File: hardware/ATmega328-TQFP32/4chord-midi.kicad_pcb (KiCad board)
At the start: 2 copper layers, 75 x 85 mm, 63 parts, among them IC1 ATMEGA328P-A, P1 USB_B, P2 Programmer, P3 UART, Q1 2N2222, SW1 <, SW2 Select, SW3 >, SW4 I, SW5 V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

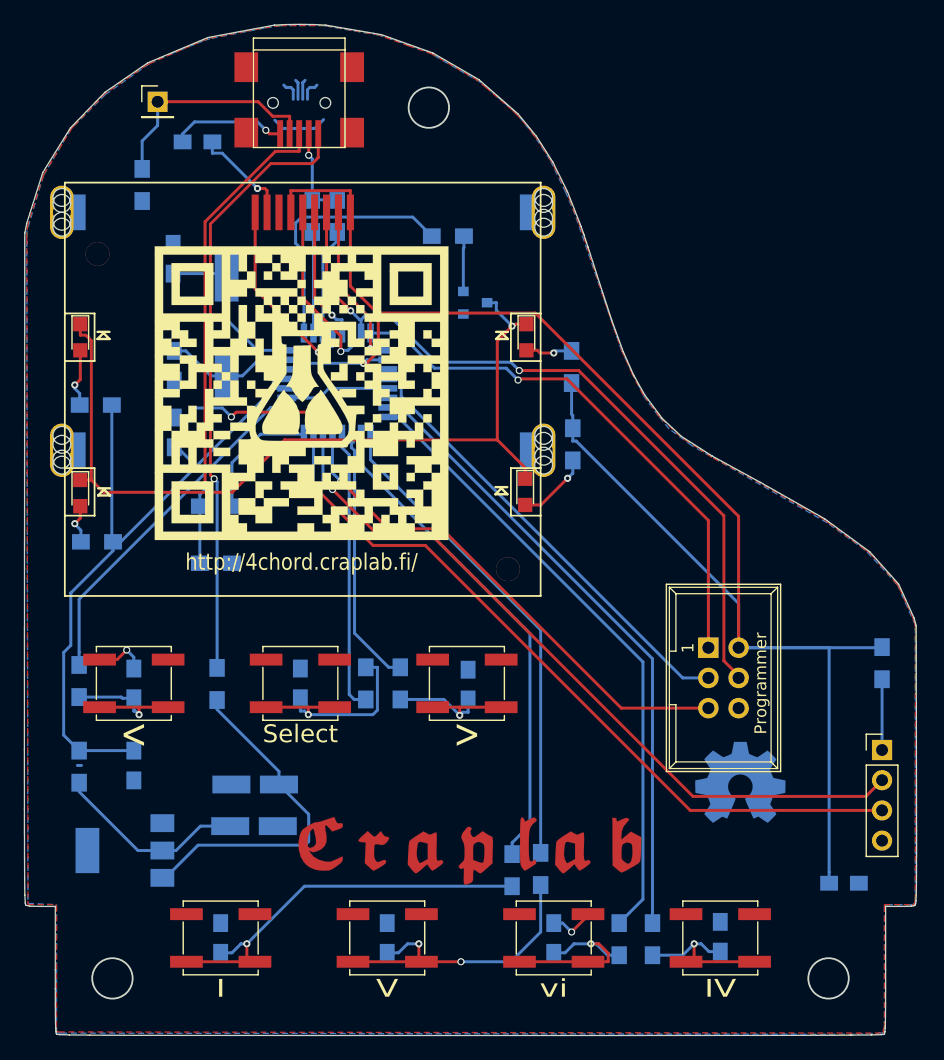
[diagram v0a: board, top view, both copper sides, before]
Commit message: issue-#13: Revised Revision B hardware
Reworked schematic to separate to logical blocks, added reset circuit,
fixed Q1 pin assignment and changed it from BJT to MOSFET component.
Also added power supply choices for UART (5V, 3.3V and none) and a
fourth rubber foot for better balance.

Obviously same changes in the PCB design, also moved button silk screen
bit more down for better readability. Fixed one sharp corner in the
board border. Improved routing somewhat.
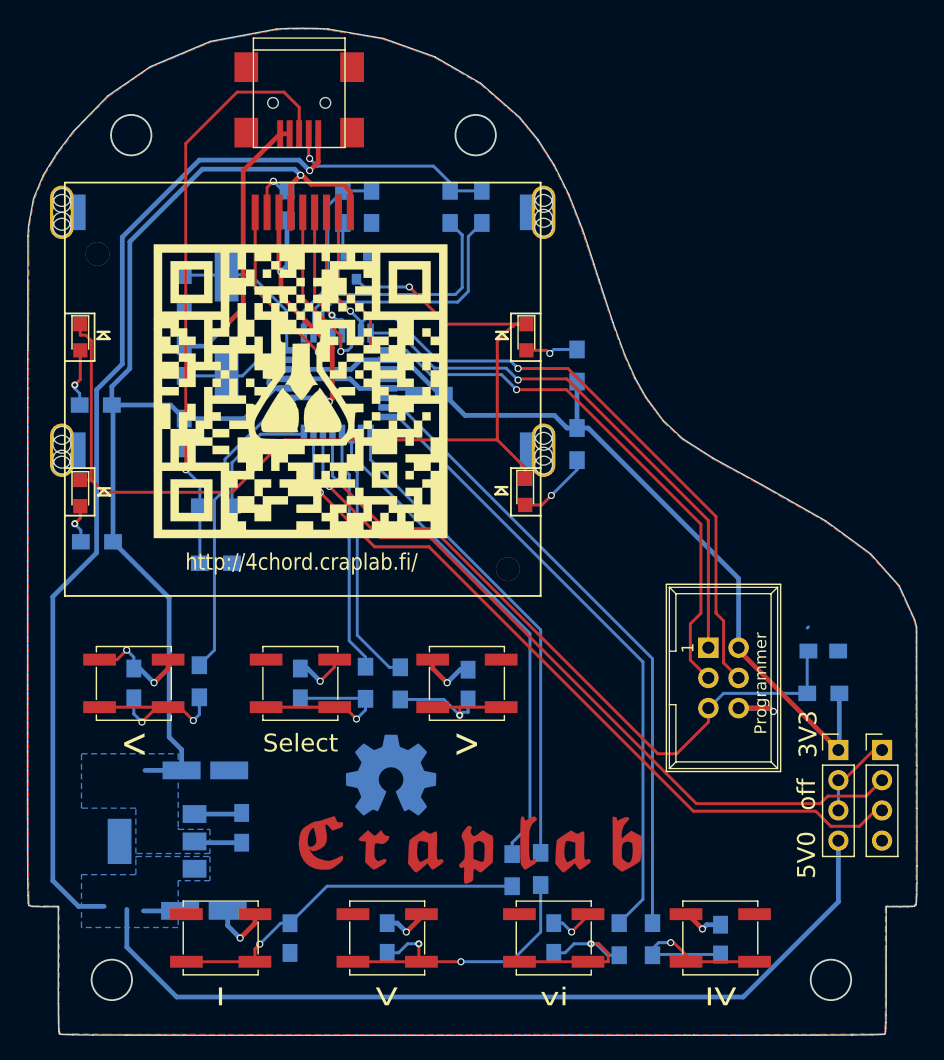
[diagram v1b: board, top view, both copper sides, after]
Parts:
- removed the G*** at (159.2, 118.8)
- removed G10: LOGO, Artwork_4chord-midi:projpage-QR-code-inv
- removed the G4 at (173.0, 121.0)
- removed the G4 at (146.2, 118.2)
- removed G5: LOGO, Artwork_4chord-midi:oshw-mask
- removed R19, R20: 0R, Resistors_SMD:R_0805_HandSoldering
- removed W1: TP, Pin_Headers:Pin_Header_Straight_1x01_Pitch2.54mm
- added C16: 100n, Capacitors_SMD:C_0805_HandSoldering, B.Cu at (180.0, 110.0)
- added G***: LOGO, Artwork_4chord-midi:craplab-2400, B.Cu at (176.5, 103.0)
- added G11: qr, Artwork_4chord-midi:projpage-QR-code-inv, F.Cu at (136.0, 88.1)
- added G12: 4chordmidi, Artwork_4chord-midi:4chord-midi, B.Cu at (142.1, 101.2)
- added G22: craplab, Artwork_4chord-midi:craplab, B.Cu at (166.0, 101.6)
- added G31: finland, Artwork_4chord-midi:finland, B.Cu at (164.0, 119.4)
- added G4: LOGO, Artwork_4chord-midi:oshw-cooper, B.Cu at (143.6, 120.4)
- added P4: UART Power, Pin_Headers:Pin_Header_Straight_1x04_Pitch2.54mm, F.Cu at (181.2, 118.3)
- G1: footprint Artwork_4chord-midi:craplab-fraktur-Cu -> Artwork_4chord-midi:craplab-fraktur-Mask
- G2: footprint Artwork_4chord-midi:craplab-fraktur-Mask -> Artwork_4chord-midi:craplab-fraktur-Cu
- G3: footprint Artwork_4chord-midi:4chord-midi -> Artwork_4chord-midi:oshw-mask
- Q1: value 2N2222 -> 2N7002
- R16: value 1k -> 100
- R17: value 0R -> 1M
- R18: value 0R -> 10k
- moved C4 53.9 mm to (146.8, 88.4), turned to 180 degrees
- moved R18 51.0 mm to (180.0, 113.5), turned to 180 degrees
- moved C3 33.7 mm to (131.1, 124.8)
- moved C5 28.2 mm to (126.2, 91.7)
- moved G3 19.4 mm to (143.6, 120.4)
- moved R17 19.4 mm to (142.0, 72.6)
- moved R3 12.2 mm to (151.3, 72.6)
- moved R1 11.6 mm to (148.6, 72.6)
- moved C1 11.5 mm to (127.9, 131.8), turned to 0 degrees
- moved Q1 10.4 mm to (140.7, 77.7), turned to 270 degrees
- moved R5 10.1 mm to (127.5, 112.5)
- moved C15 9.23 mm to (134.9, 72.5), turned to 270 degrees
- moved R16 9.16 mm to (139.6, 72.6), turned to 90 degrees
- moved C2 6.22 mm to (128.0, 120.0)
- moved C11 5.83 mm to (135.1, 134.1), turned to 270 degrees
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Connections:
- net /BTN_MENU_MINUS renamed /BTN_MENU_PREV
- net /BTN_MENU_PLUS renamed /BTN_MENU_NEXT
- C1 pad 1: Net-(C1-Pad1) -> +5V
- C2 pad 1: Net-(C2-Pad1) -> +3V3
- P1 pad 1: Net-(P1-Pad1) -> +5V
- P1 pad 4: Net-(P1-Pad4) -> GND
- Q1 pad 1: GND -> Net-(Q1-Pad1)
- Q1 pad 2: Net-(Q1-Pad2) -> GND
- R16 pad 1: Net-(Q1-Pad2) -> Net-(Q1-Pad1)
- R17 pad 1: Net-(P1-Pad4) -> /LCD_BACKLIGHT_PWM
- R18 pad 1: Net-(C1-Pad1) -> +3V3
- R18 pad 2: Net-(P1-Pad1) -> /#RESET
- U1 pad 2: Net-(C2-Pad1) -> +3V3
- U1 pad 3: Net-(C1-Pad1) -> +5V
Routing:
- net +5V: track 0.00 -> 160.6 mm, vias 0 -> 1
- net GND: track 41.9 -> 105.9 mm, vias 5 -> 12
- net Net-(P1-Pad1): track 50.9 -> 0.00 mm, vias 1 -> 0
- net +3V3: track 210.9 -> 177.7 mm
- net Net-(C1-Pad1): track 28.7 -> 0.00 mm
- net Net-(P1-Pad4): track 19.3 -> 0.00 mm
- net /#RESET: track 43.0 -> 59.9 mm
- net Net-(C2-Pad1): track 16.3 -> 0.00 mm
- net Net-(D1-Pad1): track 69.9 -> 82.5 mm
- net /USB_D-: track 8.54 -> 21.1 mm
- net /USB_RESET: track 9.00 -> 21.0 mm
- net (no net): track 11.9 -> 0.14 mm
- net Net-(P1-Pad2): track 7.77 -> 18.1 mm
- net Net-(P1-Pad3): track 40.7 -> 49.9 mm
- net /LCD_BACKLIGHT_PWM: track 21.9 -> 15.8 mm
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- added copper zone on B.Cu, net +3V3
- added copper zone on B.Cu, net +5V
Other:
- board size 75 x 85 mm -> 74.8 x 84.7 mm
- net class Power added: clearance 0.2, trace_width 0.4, via_dia 0.6, via_drill 0.4
- net class Signal added: clearance 0.2, trace_width 0.2, via_dia 0.6, via_drill 0.4
- board text added: "08-2017"
- board text added: "3V3"
- board text added: "5V0"
- board text added: "Designed in Finland, perkele!"
- board text added: "off"
- board text removed: "----------------------- Zero Ohm debug links: ----------------------- R17: GND R18: 5V USB input voltage Vbus R19: 3.3V LDO output voltage Vout ----------------------- R20: UART Vin, DNP for USB UART -----------------------"
- board text removed: "07-2017"

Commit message: issue-#15 Finalized Revision B hardware
Final little touches here and there on the PCB design, mainly silk
screen adjustments and moved the upper rubber feet.

Alos, fucked up 00f85adde54214f45f219a16524527a8af92649b which should
have been linked to issue-#15 as well. Oh well..
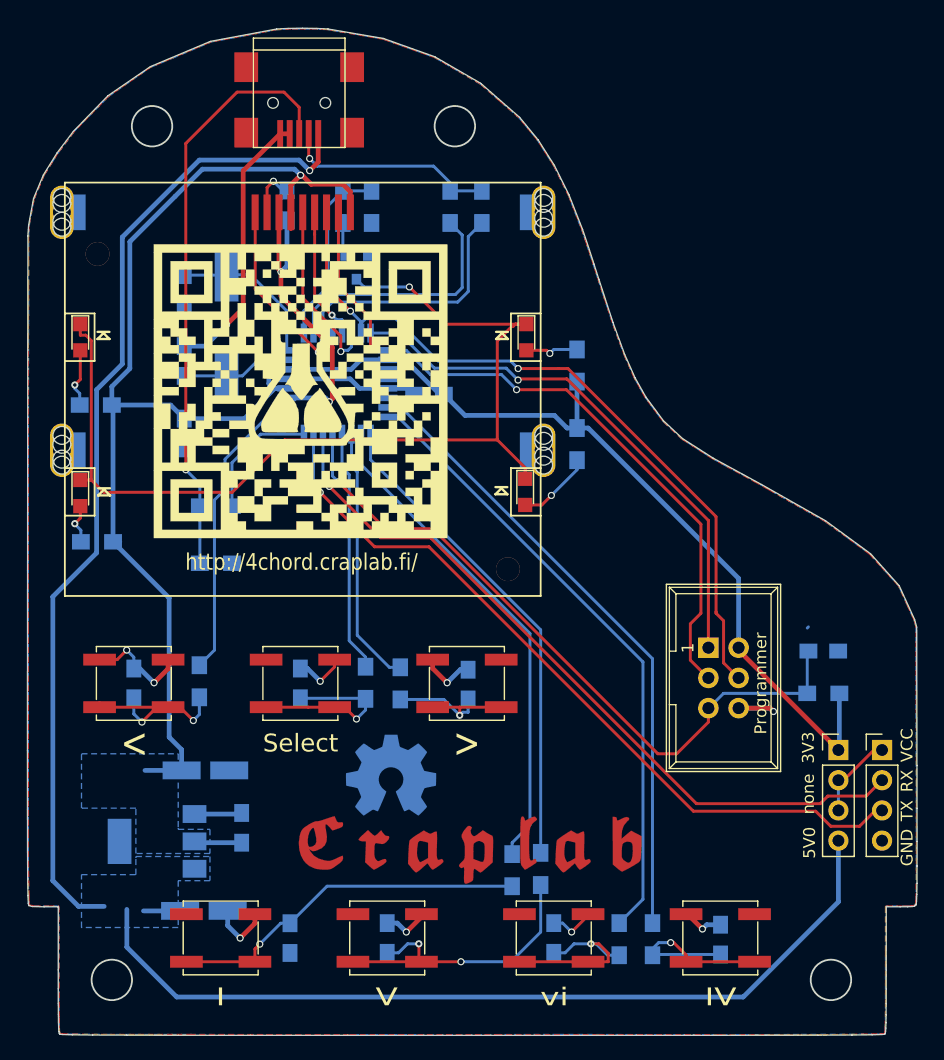
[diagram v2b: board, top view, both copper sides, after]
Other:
- outline, holes or cut-outs redrawn
- board text added: "GND"
- board text added: "RX"
- board text added: "TX"
- board text added: "VCC"
- board text added: "none"
- board text removed: "off"
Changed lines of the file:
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@@
     (area 113.004021 57.572699 187.894301 142.340801)
     (thickness 1.6)
-    (drawings 128)
+    (drawings 132)
     (tracks 471)
     (zones 0)
@@
     (zone_45_only yes)
     (trace_min 0.2)
-    (segment_width 0.2)
+    (segment_width 0.15)
     (edge_width 0.15)
     (via_size 0.6)
@@
       (xy -0.560917 0.037042)) (layer B.SilkS) (width 0.01))
   )
-  (gr_text off (at 178.562 122.047 90) (layer F.SilkS)
-    (effects (font (size 1.5 1.5) (thickness 0.3)))
+  (gr_text VCC (at 187 117.9 90) (layer F.SilkS)
+    (effects (font (size 1 1) (thickness 0.2)))
   )
-  (gr_text 3V3 (at 178.689 116.967 90) (layer F.SilkS)
-    (effects (font (size 1.5 1.5) (thickness 0.3)))
+  (gr_text RX (at 187 120.9 90) (layer F.SilkS)
+    (effects (font (size 1 1) (thickness 0.2)))
   )
-  (gr_text 5V0 (at 178.562 127.127 90) (layer F.SilkS)
-    (effects (font (size 1.5 1.5) (thickness 0.3)))
+  (gr_text TX (at 187 123.4 90) (layer F.SilkS)
+    (effects (font (size 1 1) (thickness 0.2)))
+  )
+  (gr_text GND (at 187 126.5 90) (layer F.SilkS)
+    (effects (font (size 1 1) (thickness 0.2)))
+  )
+  (gr_text none (at 178.7 122 90) (layer F.SilkS)
+    (effects (font (size 1 1) (thickness 0.2)))
+  )
+  (gr_text 3V3 (at 178.7 118.1 90) (layer F.SilkS)
+    (effects (font (size 1 1) (thickness 0.2)))
+  )
+  (gr_text 5V0 (at 178.8 126.1 90) (layer F.SilkS)
+    (effects (font (size 1 1) (thickness 0.2)))
   )
   (gr_text "Designed in Finland, perkele!" (at 158.369 109.601 90) (layer B.SilkS)
-    (effects (font (size 0.9 0.6) (thickness 0.15)) (justify left mirror))
+    (effects (font (size 0.9 0.6) (thickness 0.1)) (justify left mirror))
   )
-  (gr_circle (center 121.781 66.6114) (end 123.481 66.6114) (layer Edge.Cuts) (width 0.15))
+  (gr_circle (center 123.531 65.8614) (end 125.231 65.8614) (layer Edge.Cuts) (width 0.15))
   (gr_line (start 116.00302 142.219142) (end 115.76738 142.188825) (layer Edge.Cuts) (width 0.1))
   (gr_line (start 116.82709 142.242569) (end 116.00302 142.219142) (layer Edge.Cuts) (width 0.1))
@@
   (gr_line (start 115.73017 142.124057) (end 115.70261 141.972473) (layer Edge.Cuts) (width 0.1))
   (gr_line (start 115.76738 142.188825) (end 115.73017 142.124057) (layer Edge.Cuts) (width 0.1))
-  (gr_circle (center 150.737 66.6114) (end 152.437 66.6114) (layer Edge.Cuts) (width 0.15))
+  (gr_circle (center 148.987 65.8614) (end 150.687 65.8614) (layer Edge.Cuts) (width 0.15))
   (gr_circle (center 120.1492 137.627) (end 121.8492 137.627) (layer Edge.Cuts) (width 0.15))
   (gr_circle (center 180.6032 137.627) (end 182.3032 137.627) (layer Edge.Cuts) (width 0.15))
@@
     (effects (font (size 1.4 1.2) (thickness 0.3)))
   )
-  (gr_text "...because why not?" (at 167.767 104.902) (layer B.SilkS)
+  (gr_text "...because why not?" (at 164.25 104.75) (layer B.SilkS)
     (effects (font (size 1.2 0.8) (thickness 0.2) italic) (justify mirror))
   )
